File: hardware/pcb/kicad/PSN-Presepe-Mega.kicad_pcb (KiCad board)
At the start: 2 copper layers, 280 x 170 mm, 77 parts, among them J1 12V_IN, K1 G5Q-1_DC12, K10 G5Q-1_DC12, K11 G5Q-1_DC12, K12 G5Q-1_DC12, K13 G5Q-1_DC12, K14 G5Q-1_DC12, K15 G5Q-1_DC12, K16 G5Q-1_DC12, K2 G5Q-1_DC12, K3 G5Q-1_DC12, K4 G5Q-1_DC12, K5 G5Q-1_DC12, K6 G5Q-1_DC12, K7 G5Q-1_DC12, K8 G5Q-1_DC12, K9 G5Q-1_DC12, Q1 IRLZ44N_CIELO_R, Q2 IRLZ44N_CIELO_G, Q3 IRLZ44N_CIELO_B, Q4 IRLZ44N_TRAM_R, Q5 IRLZ44N_TRAM_G, Q6 IRLZ44N_TRAM_B, Q7 IRLZ44N_ALBA_R, Q8 IRLZ44N_ALBA_G, Q9 IRLZ44N_ALBA_B, U1 ULN2803C, U2 ULN2803C

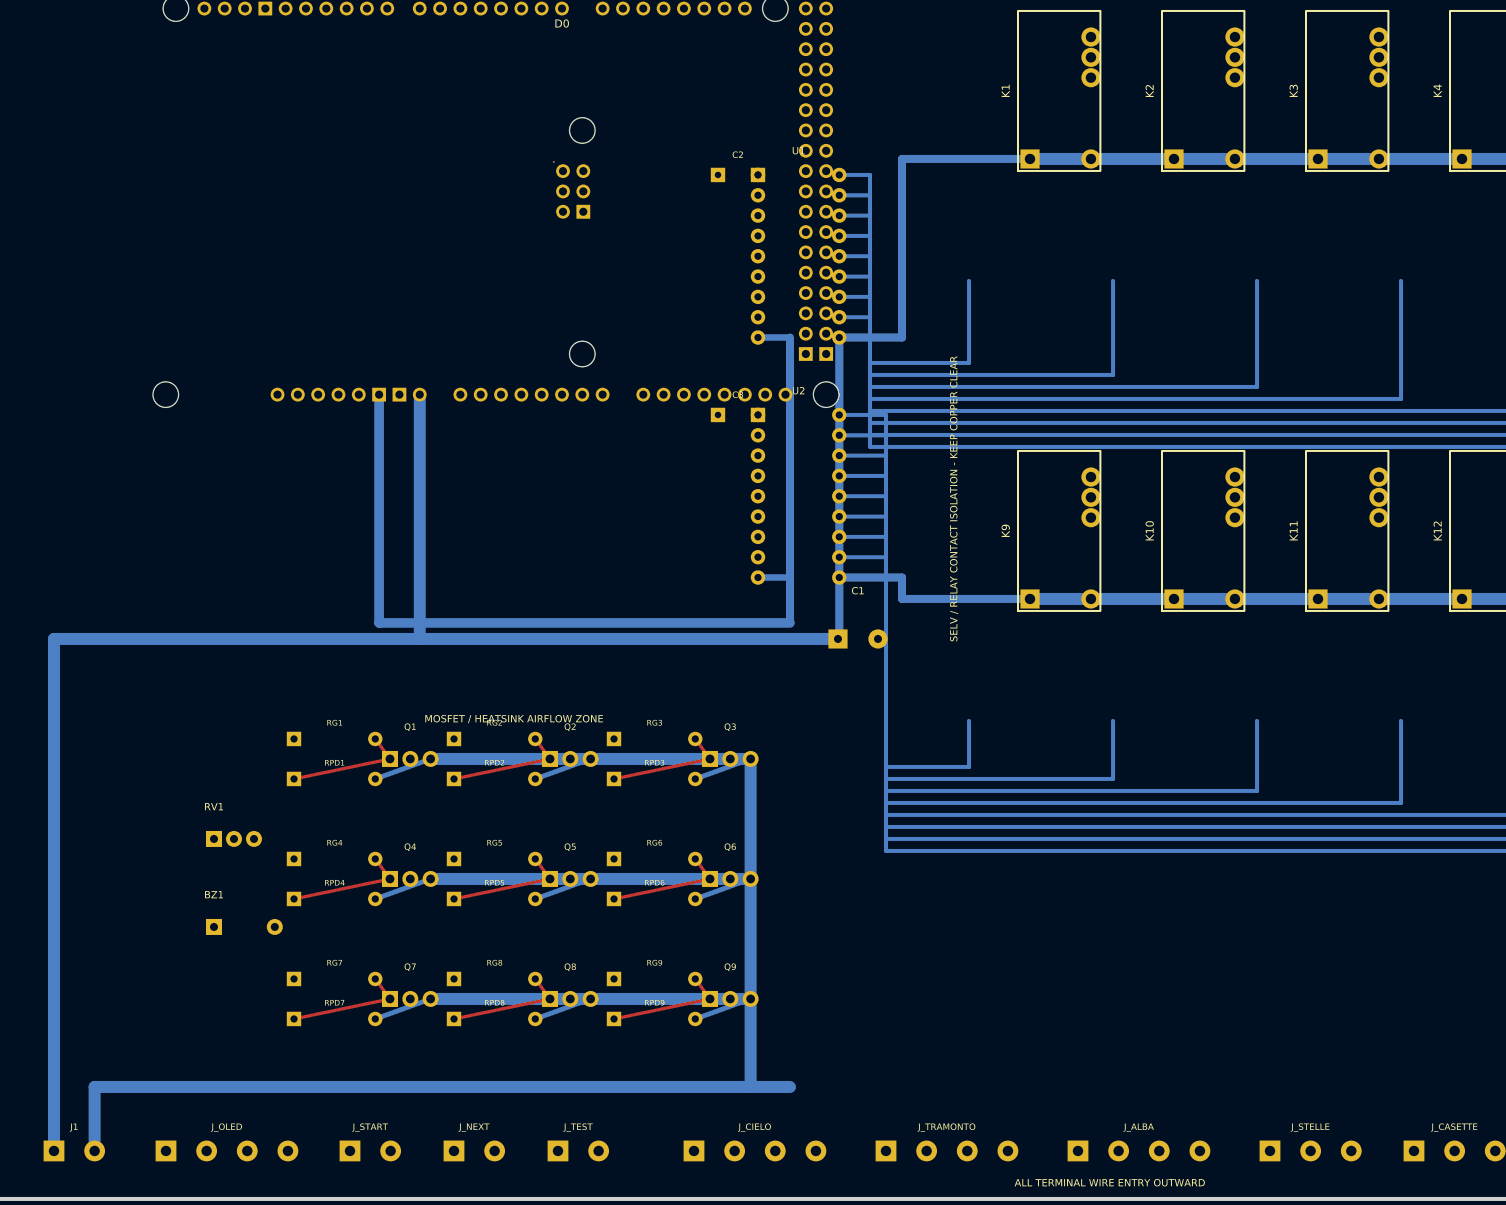
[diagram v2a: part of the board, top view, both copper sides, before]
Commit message: Route Mega relay controls and low-voltage power buses
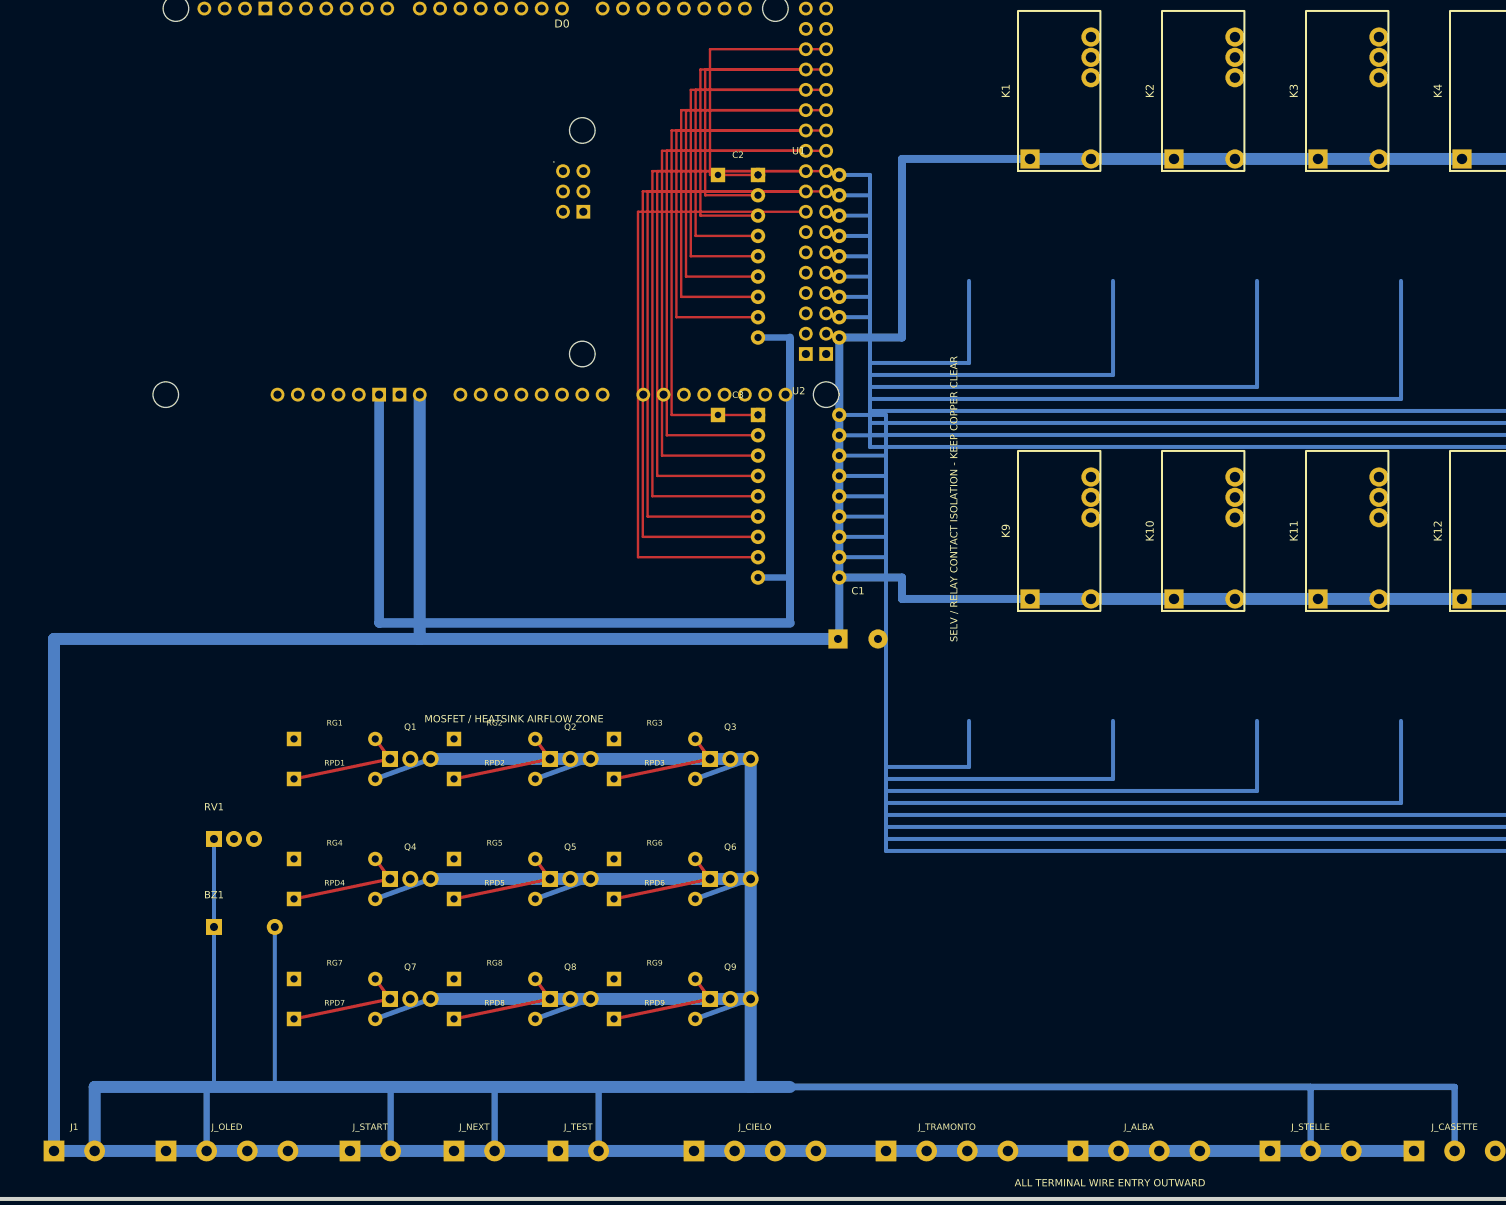
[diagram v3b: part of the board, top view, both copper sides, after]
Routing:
- net GND: track 445.7 -> 1030.7 mm
- net +12V: track 555.1 -> 725.1 mm
- net D39_RELAY15: track 0.00 -> 80.5 mm
- net D40_RELAY16: track 0.00 -> 79.2 mm
- net D37_RELAY13: track 0.00 -> 75.6 mm
- net D38_RELAY14: track 0.00 -> 74.2 mm
- net D35_RELAY11: track 0.00 -> 70.6 mm
- net D36_RELAY12: track 0.00 -> 69.3 mm
- net D33_RELAY9: track 0.00 -> 65.7 mm
- net D34_RELAY10: track 0.00 -> 64.3 mm
- net D31_RELAY7: track 0.00 -> 51.1 mm
- net D32_RELAY8: track 0.00 -> 49.7 mm
- net D29_RELAY5: track 0.00 -> 46.1 mm
- net D30_RELAY6: track 0.00 -> 44.8 mm
- net D27_RELAY3: track 0.00 -> 41.2 mm
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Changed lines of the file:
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@@
   (segment (start 132 146.5) (end 268.38 146.5) (width 0.5) (layer "B.Cu") (net 51))
   (segment (start 268.38 146.5) (end 268.38 130.24) (width 0.5) (layer "B.Cu") (net 51))
+  (segment (start 124.52 46.28) (end 110 46.28) (width 0.3) (layer "F.Cu") (net 20))
+  (segment (start 110 46.28) (end 110 62) (width 0.3) (layer "F.Cu") (net 20))
+  (segment (start 110 62) (end 116 62) (width 0.3) (layer "F.Cu") (net 20))
+  (segment (start 121.98 48.82) (end 109.4 48.82) (width 0.3) (layer "F.Cu") (net 21))
+  (segment (start 109.4 48.82) (end 109.4 64.54) (width 0.3) (layer "F.Cu") (net 21))
+  (segment (start 109.4 64.54) (end 116 64.54) (width 0.3) (layer "F.Cu") (net 21))
+  (segment (start 124.52 48.82) (end 108.8 48.82) (width 0.3) (layer "F.Cu") (net 22))
+  (segment (start 108.8 48.82) (end 108.8 67.08) (width 0.3) (layer "F.Cu") (net 22))
+  (segment (start 108.8 67.08) (end 116 67.08) (width 0.3) (layer "F.Cu") (net 22))
+  (segment (start 121.98 51.36) (end 108.2 51.36) (width 0.3) (layer "F.Cu") (net 23))
+  (segment (start 108.2 51.36) (end 108.2 69.62) (width 0.3) (layer "F.Cu") (net 23))
+  (segment (start 108.2 69.62) (end 116 69.62) (width 0.3) (layer "F.Cu") (net 23))
+  (segment (start 124.52 51.36) (end 107.6 51.36) (width 0.3) (layer "F.Cu") (net 24))
+  (segment (start 107.6 51.36) (end 107.6 72.16) (width 0.3) (layer "F.Cu") (net 24))
+  (segment (start 107.6 72.16) (end 116 72.16) (width 0.3) (layer "F.Cu") (net 24))
+  (segment (start 121.98 53.9) (end 107 53.9) (width 0.3) (layer "F.Cu") (net 25))
+  (segment (start 107 53.9) (end 107 74.7) (width 0.3) (layer "F.Cu") (net 25))
+  (segment (start 107 74.7) (end 116 74.7) (width 0.3) (layer "F.Cu") (net 25))
+  (segment (start 124.52 53.9) (end 106.4 53.9) (width 0.3) (layer "F.Cu") (net 26))
+  (segment (start 106.4 53.9) (end 106.4 77.24) (width 0.3) (layer "F.Cu") (net 26))
+  (segment (start 106.4 77.24) (end 116 77.24) (width 0.3) (layer "F.Cu") (net 26))
+  (segment (start 121.98 56.44) (end 105.8 56.44) (width 0.3) (layer "F.Cu") (net 27))
+  (segment (start 105.8 56.44) (end 105.8 79.78) (width 0.3) (layer "F.Cu") (net 27))
+  (segment (start 105.8 79.78) (end 116 79.78) (width 0.3) (layer "F.Cu") (net 27))
+  (segment (start 124.52 56.44) (end 105.2 56.44) (width 0.3) (layer "F.Cu") (net 28))
+  (segment (start 105.2 56.44) (end 105.2 92) (width 0.3) (layer "F.Cu") (net 28))
+  (segment (start 105.2 92) (end 116 92) (width 0.3) (layer "F.Cu") (net 28))
+  (segment (start 121.98 58.98) (end 104.6 58.98) (width 0.3) (layer "F.Cu") (net 29))
+  (segment (start 104.6 58.98) (end 104.6 94.54) (width 0.3) (layer "F.Cu") (net 29))
+  (segment (start 104.6 94.54) (end 116 94.54) (width 0.3) (layer "F.Cu") (net 29))
+  (segment (start 124.52 58.98) (end 104 58.98) (width 0.3) (layer "F.Cu") (net 30))
+  (segment (start 104 58.98) (end 104 97.08) (width 0.3) (layer "F.Cu") (net 30))
+  (segment (start 104 97.08) (end 116 97.08) (width 0.3) (layer "F.Cu") (net 30))
+  (segment (start 121.98 61.52) (end 103.4 61.52) (width 0.3) (layer "F.Cu") (net 31))
+  (segment (start 103.4 61.52) (end 103.4 99.62) (width 0.3) (layer "F.Cu") (net 31))
+  (segment (start 103.4 99.62) (end 116 99.62) (width 0.3) (layer "F.Cu") (net 31))
+  (segment (start 124.52 61.52) (end 102.8 61.52) (width 0.3) (layer "F.Cu") (net 32))
+  (segment (start 102.8 61.52) (end 102.8 102.16) (width 0.3) (layer "F.Cu") (net 32))
+  (segment (start 102.8 102.16) (end 116 102.16) (width 0.3) (layer "F.Cu") (net 32))
+  (segment (start 121.98 64.06) (end 102.2 64.06) (width 0.3) (layer "F.Cu") (net 33))
+  (segment (start 102.2 64.06) (end 102.2 104.7) (width 0.3) (layer "F.Cu") (net 33))
+  (segment (start 102.2 104.7) (end 116 104.7) (width 0.3) (layer "F.Cu") (net 33))
+  (segment (start 124.52 64.06) (end 101.6 64.06) (width 0.3) (layer "F.Cu") (net 34))
+  (segment (start 101.6 64.06) (end 101.6 107.24) (width 0.3) (layer "F.Cu") (net 34))
+  (segment (start 101.6 107.24) (end 116 107.24) (width 0.3) (layer "F.Cu") (net 34))
+  (segment (start 121.98 66.6) (end 101 66.6) (width 0.3) (layer "F.Cu") (net 35))
+  (segment (start 101 66.6) (end 101 109.78) (width 0.3) (layer "F.Cu") (net 35))
+  (segment (start 101 109.78) (end 116 109.78) (width 0.3) (layer "F.Cu") (net 35))
+  (segment (start 28 184) (end 198 184) (width 1.5) (layer "B.Cu") (net 2))
+  (segment (start 47.08 184) (end 47.08 176) (width 0.8) (layer "B.Cu") (net 1))
+  (segment (start 47.08 176) (end 33.08 176) (width 0.8) (layer "B.Cu") (net 1))
+  (segment (start 70.08 184) (end 70.08 176) (width 0.8) (layer "B.Cu") (net 1))
+  (segment (start 70.08 176) (end 33.08 176) (width 0.8) (layer "B.Cu") (net 1))
+  (segment (start 83.08 184) (end 83.08 176) (width 0.8) (layer "B.Cu") (net 1))
+  (segment (start 83.08 176) (end 33.08 176) (width 0.8) (layer "B.Cu") (net 1))
+  (segment (start 96.08 184) (end 96.08 176) (width 0.8) (layer "B.Cu") (net 1))
+  (segment (start 96.08 176) (end 33.08 176) (width 0.8) (layer "B.Cu") (net 1))
+  (segment (start 185.08 184) (end 185.08 176) (width 0.8) (layer "B.Cu") (net 1))
+  (segment (start 185.08 176) (end 33.08 176) (width 0.8) (layer "B.Cu") (net 1))
+  (segment (start 203.08 184) (end 203.08 176) (width 0.8) (layer "B.Cu") (net 1))
+  (segment (start 203.08 176) (end 33.08 176) (width 0.8) (layer "B.Cu") (net 1))
+  (segment (start 48 145) (end 48 176) (width 0.5) (layer "B.Cu") (net 1))
+  (segment (start 55.6 156) (end 55.6 176) (width 0.5) (layer "B.Cu") (net 1))
 )

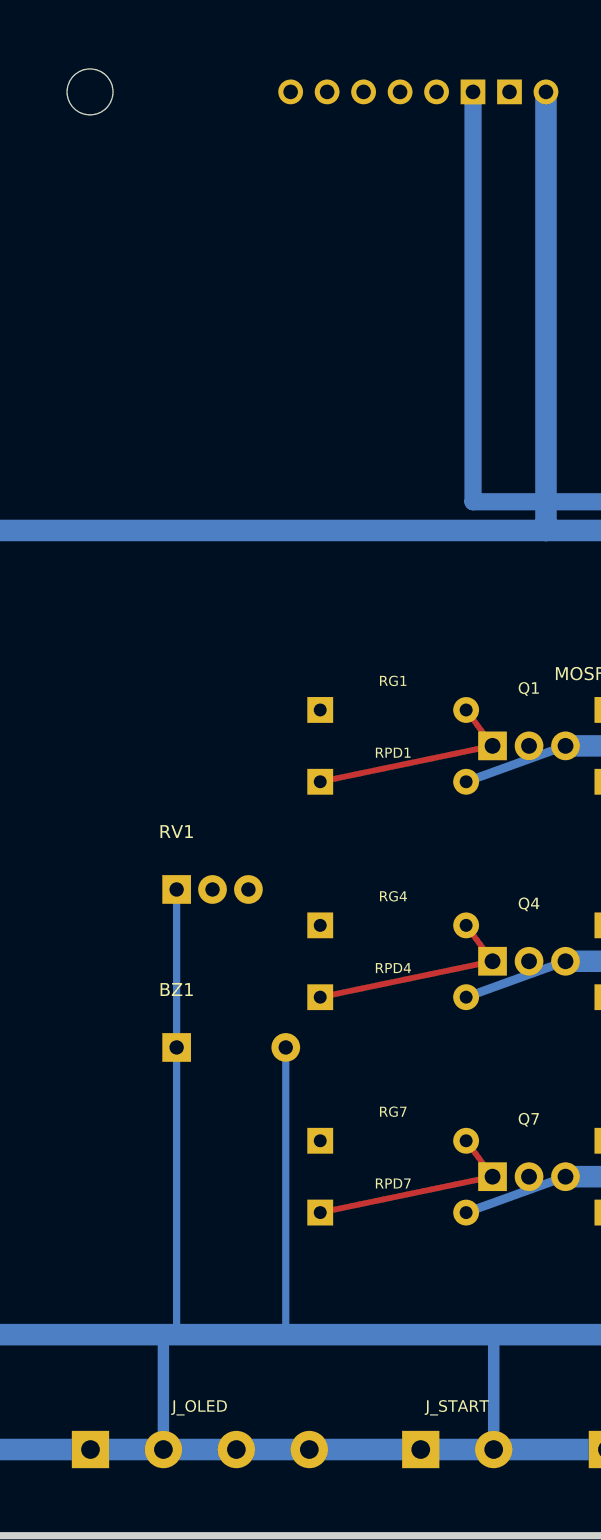
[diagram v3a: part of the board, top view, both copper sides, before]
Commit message: Connect Mega 5V and ground power nets
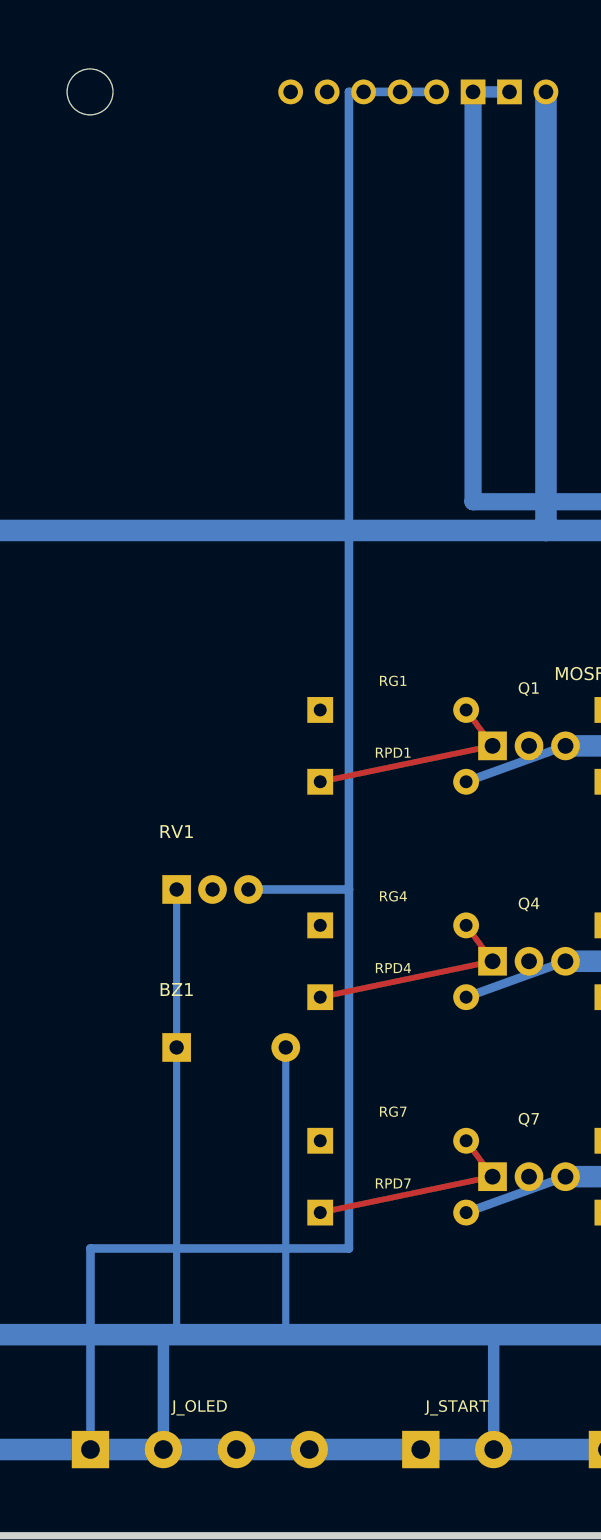
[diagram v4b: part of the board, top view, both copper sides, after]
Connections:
- MCU1 pad 5V1: (no net) -> +5V_MEGA
- MCU1 pad 5V2: (no net) -> +5V_MEGA
- MCU1 pad 5V3: (no net) -> +5V_MEGA
- MCU1 pad 5V4: (no net) -> +5V_MEGA
- MCU1 pad GND1: (no net) -> GND
- MCU1 pad GND2: (no net) -> GND
- MCU1 pad GND3: (no net) -> GND
- MCU1 pad GND4: (no net) -> GND
- MCU1 pad GND5: (no net) -> GND
- MCU1 pad GND6: (no net) -> GND
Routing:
- net +5V_MEGA: track 0.00 -> 125.6 mm
- net GND: track 1030.7 -> 1033.3 mm
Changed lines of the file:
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@@
     (pad "" thru_hole oval (at 27.94 -2.54) (size 1.7272 1.7272) (drill 1.016) (layers *.Cu *.Mask))
     (pad "3V3" thru_hole oval (at 35.56 -2.54) (size 1.7272 1.7272) (drill 1.016) (layers *.Cu *.Mask))
-    (pad "5V1" thru_hole oval (at 38.1 -2.54) (size 1.7272 1.7272) (drill 1.016) (layers *.Cu *.Mask))
-    (pad "5V2" thru_hole oval (at 66.167 -30.48) (size 1.7272 1.7272) (drill 1.016) (layers *.Cu *.Mask))
-    (pad "5V3" thru_hole oval (at 93.98 -50.8) (size 1.7272 1.7272) (drill 1.016) (layers *.Cu *.Mask))
-    (pad "5V4" thru_hole oval (at 96.52 -50.8) (size 1.7272 1.7272) (drill 1.016) (layers *.Cu *.Mask))
+    (pad "5V1" thru_hole oval (at 38.1 -2.54) (size 1.7272 1.7272) (drill 1.016) (layers *.Cu *.Mask) (net 52 "+5V_MEGA"))
+    (pad "5V2" thru_hole oval (at 66.167 -30.48) (size 1.7272 1.7272) (drill 1.016) (layers *.Cu *.Mask) (net 52 "+5V_MEGA"))
+    (pad "5V3" thru_hole oval (at 93.98 -50.8) (size 1.7272 1.7272) (drill 1.016) (layers *.Cu *.Mask) (net 52 "+5V_MEGA"))
+    (pad "5V4" thru_hole oval (at 96.52 -50.8) (size 1.7272 1.7272) (drill 1.016) (layers *.Cu *.Mask) (net 52 "+5V_MEGA"))
     (pad "A0" thru_hole oval (at 50.8 -2.54) (size 1.7272 1.7272) (drill 1.016) (layers *.Cu *.Mask (net 19 "A0_POT")))
     (pad "A1" thru_hole oval (at 53.34 -2.54) (size 1.7272 1.7272) (drill 1.016) (layers *.Cu *.Mask))
@@
     (pad "D52" thru_hole oval (at 93.98 -10.16) (size 1.7272 1.7272) (drill 1.016) (layers *.Cu *.Mask))
     (pad "D53" thru_hole oval (at 96.52 -10.16) (size 1.7272 1.7272) (drill 1.016) (layers *.Cu *.Mask))
-    (pad "GND1" thru_hole rect (at 26.416 -50.8) (size 1.7272 1.7272) (drill 1.016) (layers *.Cu *.Mask))
-    (pad "GND2" thru_hole rect (at 40.64 -2.54) (size 1.7272 1.7272) (drill 1.016) (layers *.Cu *.Mask))
-    (pad "GND3" thru_hole rect (at 43.18 -2.54) (size 1.7272 1.7272) (drill 1.016) (layers *.Cu *.Mask))
-    (pad "GND4" thru_hole rect (at 66.167 -25.4) (size 1.7272 1.7272) (drill 1.016) (layers *.Cu *.Mask))
-    (pad "GND5" thru_hole rect (at 93.98 -7.62) (size 1.7272 1.7272) (drill 1.016) (layers *.Cu *.Mask))
-    (pad "GND6" thru_hole rect (at 96.52 -7.62) (size 1.7272 1.7272) (drill 1.016) (layers *.Cu *.Mask))
+    (pad "GND1" thru_hole rect (at 26.416 -50.8) (size 1.7272 1.7272) (drill 1.016) (layers *.Cu *.Mask) (net 1 "GND"))
+    (pad "GND2" thru_hole rect (at 40.64 -2.54) (size 1.7272 1.7272) (drill 1.016) (layers *.Cu *.Mask) (net 1 "GND"))
+    (pad "GND3" thru_hole rect (at 43.18 -2.54) (size 1.7272 1.7272) (drill 1.016) (layers *.Cu *.Mask) (net 1 "GND"))
+    (pad "GND4" thru_hole rect (at 66.167 -25.4) (size 1.7272 1.7272) (drill 1.016) (layers *.Cu *.Mask) (net 1 "GND"))
+    (pad "GND5" thru_hole rect (at 93.98 -7.62) (size 1.7272 1.7272) (drill 1.016) (layers *.Cu *.Mask) (net 1 "GND"))
+    (pad "GND6" thru_hole rect (at 96.52 -7.62) (size 1.7272 1.7272) (drill 1.016) (layers *.Cu *.Mask) (net 1 "GND"))
     (pad "IORF" thru_hole oval (at 30.48 -2.54) (size 1.7272 1.7272) (drill 1.016) (layers *.Cu *.Mask))
     (pad "MISO" thru_hole oval (at 63.627 -30.48) (size 1.7272 1.7272) (drill 1.016) (layers *.Cu *.Mask))
@@
   (segment (start 48 145) (end 48 176) (width 0.5) (layer "B.Cu") (net 1))
   (segment (start 55.6 156) (end 55.6 176) (width 0.5) (layer "B.Cu") (net 1))
+  (segment (start 66.1 89.46) (end 60 89.46) (width 0.6) (layer "B.Cu") (net 52))
+  (segment (start 60 89.46) (end 60 145) (width 0.6) (layer "B.Cu") (net 52))
+  (segment (start 60 145) (end 53 145) (width 0.6) (layer "B.Cu") (net 52))
+  (segment (start 60 145) (end 60 170) (width 0.6) (layer "B.Cu") (net 52))
+  (segment (start 60 170) (end 42 170) (width 0.6) (layer "B.Cu") (net 52))
+  (segment (start 42 170) (end 42 184) (width 0.6) (layer "B.Cu") (net 52))
+  (segment (start 68.64 89.46) (end 71.18 89.46) (width 0.8) (layer "B.Cu") (net 1))
 )
